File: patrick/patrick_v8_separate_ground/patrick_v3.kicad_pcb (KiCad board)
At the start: 2 copper layers, 21 x 13 mm, 19 parts, among them J1 Conn_02x05_Counter_Clockwise, J2 Conn_01x01, J3 Conn_01x01, J4 Conn_01x01, J5 Conn_01x01, J6 Conn_01x01, J7 Conn_01x05, Q1 Q_NMOS_GSD, Q2 Q_NMOS_GSD, Q3 Q_NMOS_GSD, Q4 Q_NMOS_GSD

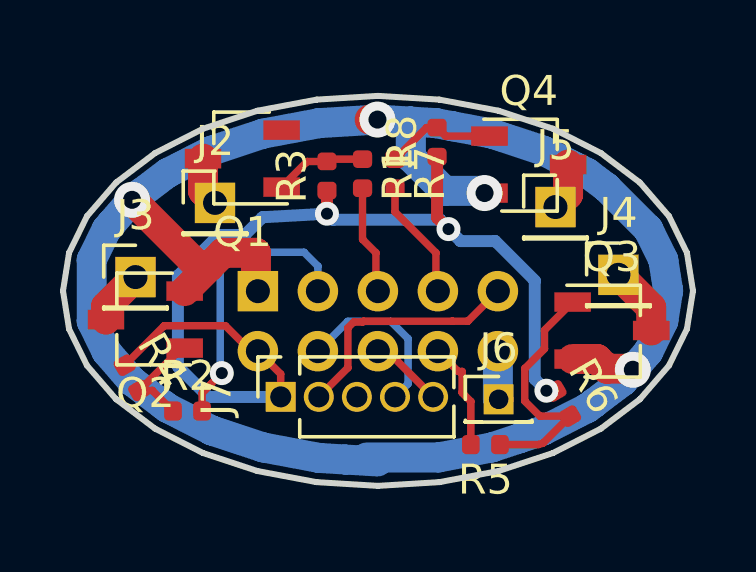
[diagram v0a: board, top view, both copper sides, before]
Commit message: separate gnd
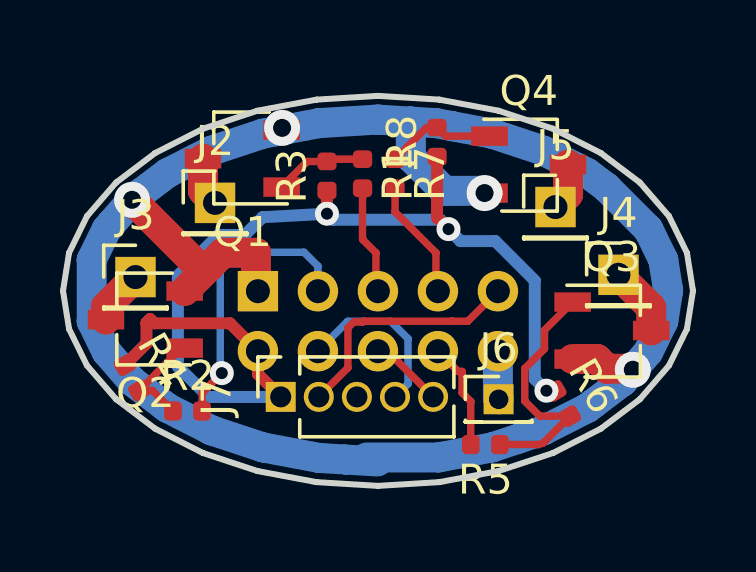
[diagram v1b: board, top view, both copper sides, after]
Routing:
- net GND2: track 35.3 -> 36.1 mm
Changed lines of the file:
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@@
-(kicad_pcb (version 20171130) (host pcbnew 5.1.7-a382d34a88~90~ubuntu20.04.1)
+(kicad_pcb (version 20171130) (host pcbnew 5.1.10-88a1d61d58~88~ubuntu18.04.1)
   (general
     (thickness 1.6)
     (drawings 128)
-    (tracks 178)
+    (tracks 180)
     (zones 0)
     (modules 19)
@@
   (gr_line (start 164.12205 110.707363) (end 165.092355 109.583599) (layer Edge.Cuts) (width 0.2))
   (gr_line (start 165.689865 105.82807) (end 165.092355 104.608715) (layer Edge.Cuts) (width 0.2))
-  (via (at 161.00552 110.42396) (size 0.8) (drill 0.4) (layers F.Cu B.Cu) (net 19))
   (segment (start 162.057467 103.009313) (end 160.898769 102.420651) (width 1) (layer B.Cu) (net 1))
   (segment (start 162.573226 110.848666) (end 163.554475 110.1085) (width 1) (layer B.Cu) (net 1))
@@
   (via (at 158.94304 103.8352) (size 1.2) (drill 0.6) (layers F.Cu B.Cu) (net 1))
   (segment (start 155.373864 101.386139) (end 153.423969 101.505024) (width 1) (layer B.Cu) (net 1))
-  (via (at 155.373864 101.386139) (size 1.2) (drill 0.6) (layers F.Cu B.Cu) (net 1))
+  (via (at 152.19426 101.6635) (size 1.2) (drill 0.6) (layers F.Cu B.Cu) (net 1))
   (segment (start 156.485618 102.645238) (end 157.60192 103.76154) (width 1) (layer B.Cu) (net 1))
   (segment (start 156.485618 101.453922) (end 156.485618 102.645238) (width 1) (layer B.Cu) (net 1))
   (segment (start 157.323759 101.505025) (end 156.485618 101.453922) (width 1) (layer B.Cu) (net 1))
   (segment (start 156.485618 101.453922) (end 155.458577 101.391303) (width 1) (layer B.Cu) (net 1))
-  (segment (start 155.113071 101.386139) (end 155.373864 101.386139) (width 1) (layer F.Cu) (net 1))
   (segment (start 151.32354 105.82656) (end 150.22322 105.82656) (width 1) (layer F.Cu) (net 1))
   (segment (start 147.193255 104.060784) (end 146.498527 104.865387) (width 1) (layer B.Cu) (net 1))
@@
   (segment (start 153.38806 106.27106) (end 152.92578 105.80878) (width 0.25) (layer B.Cu) (net 18))
   (segment (start 153.38806 107.10672) (end 153.38806 106.27106) (width 0.25) (layer B.Cu) (net 18))
-  (segment (start 146.94796 109.574678) (end 148.26488 108.257758) (width 0.25) (layer F.Cu) (net 19))
+  (via (at 161.00552 110.42396) (size 0.8) (drill 0.4) (layers F.Cu B.Cu) (net 19))
   (segment (start 151.153044 109.10672) (end 151.38806 109.10672) (width 0.25) (layer F.Cu) (net 19))
-  (segment (start 150.304082 108.257758) (end 151.153044 109.10672) (width 0.25) (layer F.Cu) (net 19))
-  (segment (start 148.26488 108.257758) (end 150.304082 108.257758) (width 0.25) (layer F.Cu) (net 19))
-  (segment (start 152.14854 109.8672) (end 151.38806 109.10672) (width 0.25) (layer F.Cu) (net 19))
-  (segment (start 152.14854 110.6297) (end 152.14854 109.8672) (width 0.25) (layer F.Cu) (net 19))
   (segment (start 152.146019 110.632221) (end 149.738061 110.632221) (width 0.4) (layer B.Cu) (net 19))
   (segment (start 152.14854 110.6297) (end 152.146019 110.632221) (width 0.4) (layer B.Cu) (net 19))
@@
   (segment (start 161.013836 110.432276) (end 161.00552 110.42396) (width 0.4) (layer F.Cu) (net 19))
   (segment (start 161.30792 110.432276) (end 161.013836 110.432276) (width 0.4) (layer F.Cu) (net 19))
+  (segment (start 151.38806 109.86922) (end 152.14854 110.6297) (width 0.4) (layer F.Cu) (net 19))
+  (segment (start 151.38806 109.10672) (end 151.38806 109.86922) (width 0.4) (layer F.Cu) (net 19))
+  (segment (start 146.94796 109.574678) (end 147.67306 108.849578) (width 0.4) (layer F.Cu) (net 19))
+  (segment (start 147.67306 108.849578) (end 147.67306 108.15574) (width 0.4) (layer F.Cu) (net 19))
+  (segment (start 147.67306 108.15574) (end 147.79498 108.03382) (width 0.4) (layer F.Cu) (net 19))
+  (segment (start 150.458061 108.176721) (end 151.38806 109.10672) (width 0.4) (layer F.Cu) (net 19))
+  (segment (start 147.937881 108.176721) (end 150.458061 108.176721) (width 0.4) (layer F.Cu) (net 19))
+  (segment (start 147.79498 108.03382) (end 147.937881 108.176721) (width 0.4) (layer F.Cu) (net 19))
 )
